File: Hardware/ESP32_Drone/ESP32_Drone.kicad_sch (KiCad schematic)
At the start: 71 parts, among them J1 USB_C_Receptacle_USB2.0_16P, J2 Conn_01x02_Socket, J3 Conn_01x02_Socket, J4 Conn_01x02_Socket, J5 Conn_01x02_Socket, J6 Conn_01x02_Socket, Q1 AO3401A, Q2 SS8050, Q3 SS8050, Q4 AO3400A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

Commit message: JCSC field added.
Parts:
- C1, C12: LCSC (none) -> C15850
- C10: LCSC (none) -> C45783
- C11, C13, C14, C15, C16, C4, C6, C8, C9: LCSC (none) -> C49678
- C2: LCSC (none) -> C1740
- C3: LCSC (none) -> C1806
- C5: LCSC (none) -> C1822
- C7: LCSC (none) -> C1653
- D1: LCSC (none) -> C8599
- D10, D11, D8, D9: LCSC (none) -> C8598
- D2: LCSC (none) -> C2286
- D3: LCSC (none) -> C2297
- J1: LCSC (none) -> C165948
- J2: LCSC (none) -> C166021
- Q1: LCSC (none) -> C15127
- Q2, Q3: LCSC (none) -> C181090
- Q4, Q5, Q6, Q7: LCSC (none) -> C20917
- R10, R11: LCSC (none) -> C21189
- R12, R13, R16, R21, R23, R25, R27, R28, R29: LCSC (none) -> C25804
- R14, R15: LCSC (none) -> C4184
- R17: LCSC (none) -> C22978
- R18, R19: LCSC (none) -> C4182
- R20, R22, R24, R26: LCSC (none) -> C21190
- R3, R4, R5, R6: LCSC (none) -> C25803
- R30, R31: LCSC (none) -> C23186
- R7: value 2k -> 1k; LCSC (none) -> C22706
- R8: value 22.1k -> 22k; LCSC (none) -> C25879
- R9: value 47.5k -> 47k; LCSC (none) -> C25819
- SW1: LCSC (none) -> JS102011SAQN
- U1: LCSC (none) -> C89366
- U2: LCSC (none) -> C2652470
- U3: LCSC (none) -> C24112
- U4: LCSC (none) -> C473012
- U5: LCSC (none) -> C16581

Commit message: PCB layout v1.0
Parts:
- C7: LCSC C1653 -> C107146
- D1: LCSC C8599 -> C8678
- D10, D11, D8, D9: LCSC C8598 -> C50645
- D3: LCSC C2297 -> C12624
- J2: LCSC C166021 -> C173752
- R18, R19: value 1.3k -> 1k; LCSC C4182 -> C21190
- R7: LCSC C22706 -> C21190
- R8: LCSC C25879 -> C23344
- SW1: LCSC JS102011SAQN -> C221660
- U1: LCSC C89366 -> C29613
- U2: LCSC C2652470 -> C964632
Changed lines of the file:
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@@
 			)
 		)
-		(property "LCSC" "C8598"
+		(property "LCSC" "C50645 "
 			(at 54.61 224.79 90)
 			(hide yes)
@@
 			)
 		)
-		(property "LCSC" "C2297"
+		(property "LCSC" "C12624"
 			(at 285.75 48.26 0)
 			(hide yes)
@@
 			)
 		)
-		(property "Value" "1.3k"
+		(property "Value" "1k"
 			(at 302.26 41.91 90)
 			(show_name no)
@@
 			)
 		)
-		(property "LCSC" "C4182"
+		(property "LCSC" "C21190"
 			(at 302.26 45.72 90)
 			(hide yes)
@@
 			)
 		)
-		(property "LCSC" "C8598"
+		(property "LCSC" "C50645 "
 			(at 250.19 224.79 90)
 			(hide yes)
@@
 			)
 		)
-		(property "LCSC" "C8598"
+		(property "LCSC" "C50645 "
 			(at 189.23 224.79 90)
 			(hide yes)
@@
 			)
 		)
-		(property "LCSC" "C1653"
+		(property "LCSC" "C107146 "
 			(at 224.79 127 0)
 			(hide yes)
@@
 			)
 		)
-		(property "LCSC" "C22706"
+		(property "LCSC" "C21190"
 			(at 46.99 114.3 90)
 			(hide yes)
@@
 			)
 		)
-		(property "LCSC" "C8598"
+		(property "LCSC" "C50645 "
 			(at 121.92 226.06 90)
 			(hide yes)
@@
 			)
 		)
-		(property "Value" "1.3k"
+		(property "Value" "1k"
 			(at 295.91 44.45 90)
 			(show_name no)
@@
 			)
 		)
-		(property "LCSC" "C4182"
+		(property "LCSC" "C21190"
 			(at 295.91 48.26 90)
 			(hide yes)
@@
 			)
 		)
-		(property "LCSC" "C25879"
+		(property "LCSC" "C23344"
 			(at 30.48 120.65 0)
 			(hide yes)
@@
 			)
 		)
-		(property "LCSC" "JS102011SAQN"
+		(property "LCSC" "C221660 "
 			(at 251.46 46.99 0)
 			(hide yes)
@@
 			)
 		)
-		(property "LCSC" "C8599"
+		(property "LCSC" "C8678"
 			(at 114.3 44.45 0)
 			(hide yes)
@@
 			)
 		)
-		(property "LCSC" "C2652470"
+		(property "LCSC" "C964632"
 			(at 66.04 142.24 0)
 			(hide yes)
@@
 			)
 		)
-		(property "LCSC" "C166021"
+		(property "LCSC" "C173752"
 			(at 369.57 40.64 0)
 			(hide yes)
@@
 			)
 		)
-		(property "LCSC" "C89366"
+		(property "LCSC" "C29613 "
 			(at 152.4 46.99 0)
 			(hide yes)

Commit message: JCSC numbers updated.
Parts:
- C2: LCSC C1740 -> C1743
- C3: LCSC C1806 -> C377773
- C5: LCSC C1822 -> C1779
- C7: LCSC C107146 -> C28260
- D3: LCSC C12624 -> C2290
- Q2, Q3: LCSC C181090 -> C2150
- R8: LCSC C23344 -> C31850
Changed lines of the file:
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@@
 			)
 		)
-		(property "LCSC" "C12624"
+		(property "LCSC" "C2290"
 			(at 285.75 48.26 0)
 			(hide yes)
@@
 			)
 		)
-		(property "LCSC" "C1740"
+		(property "LCSC" "C1743"
 			(at 163.83 53.34 0)
 			(hide yes)
@@
 			)
 		)
-		(property "LCSC" "C107146 "
+		(property "LCSC" "C28260"
 			(at 224.79 127 0)
 			(hide yes)
@@
 			)
 		)
-		(property "LCSC" "C181090"
+		(property "LCSC" "C2150"
 			(at 132.08 158.75 0)
 			(hide yes)
@@
 			)
 		)
-		(property "LCSC" "C181090"
+		(property "LCSC" "C2150"
 			(at 132.08 134.62 0)
 			(hide yes)
@@
 			)
 		)
-		(property "LCSC" "C1806"
+		(property "LCSC" "C377773"
 			(at 175.26 48.26 0)
 			(hide yes)
@@
 			)
 		)
-		(property "LCSC" "C23344"
+		(property "LCSC" "C31850"
 			(at 30.48 120.65 0)
 			(hide yes)
@@
 			)
 		)
-		(property "LCSC" "C1822"
+		(property "LCSC" "C1779"
 			(at 71.12 96.52 0)
 			(hide yes)

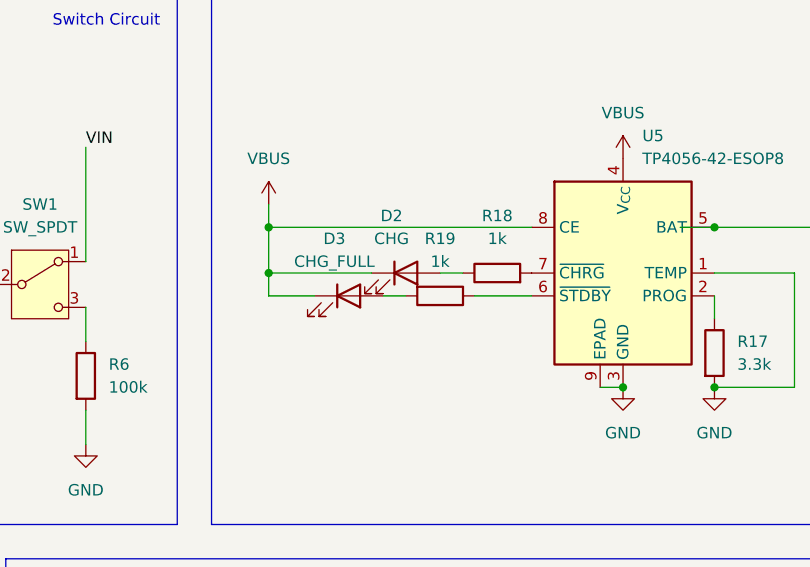
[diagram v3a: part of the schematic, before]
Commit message: Fixed charger LEDs.
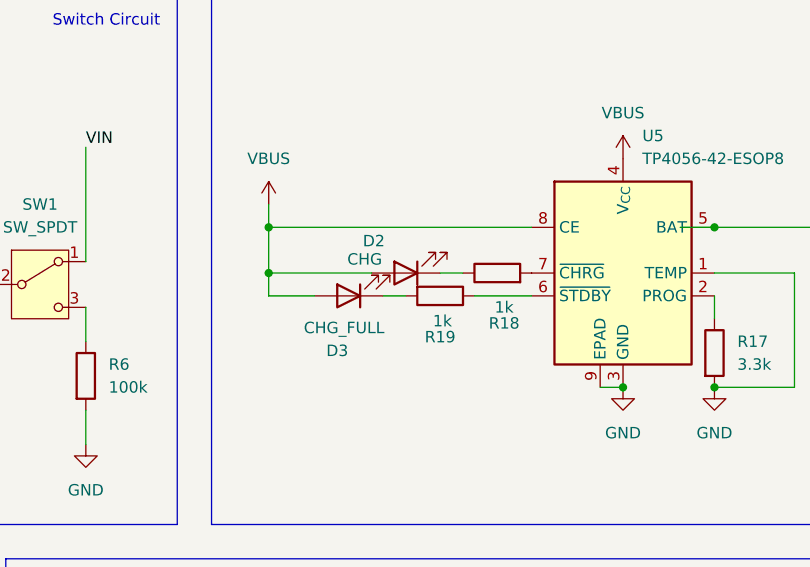
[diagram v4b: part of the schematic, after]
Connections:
- net VBUS: now also D2.2 (A), D3.2 (A); no longer D2.1 (K), D3.1 (K)
- net at R19.2: now also D3.1 (K); no longer D3.2 (A)
- net at R18.1: now also D2.1 (K); no longer D2.2 (A)
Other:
- moved on the sheet: D2, D3
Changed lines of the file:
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@@
 	(symbol
 		(lib_id "Device:LED")
-		(at 285.75 48.26 0)
+		(at 285.75 48.26 180)
 		(unit 1)
 		(body_style 1)
@@
 		(in_pos_files yes)
 		(dnp no)
-		(fields_autoplaced yes)
 		(property "Reference" "D3"
-			(at 284.1625 41.91 0)
+			(at 284.48 54.356 0)
 			(show_name no)
 			(do_not_autoplace no)
@@
 		)
 		(property "Value" "CHG_FULL"
-			(at 284.1625 44.45 0)
+			(at 285.242 51.816 0)
 			(show_name no)
 			(do_not_autoplace no)
@@
 		(in_pos_files yes)
 		(dnp no)
-		(fields_autoplaced yes)
 		(property "Reference" "R18"
-			(at 302.26 39.37 90)
+			(at 303.022 51.308 90)
 			(show_name no)
 			(do_not_autoplace no)
@@
 		)
 		(property "Value" "1k"
-			(at 302.26 41.91 90)
+			(at 303.022 49.53 90)
 			(show_name no)
 			(do_not_autoplace no)
@@
 	(symbol
 		(lib_id "Device:LED")
-		(at 292.1 45.72 0)
+		(at 292.1 45.72 180)
 		(unit 1)
 		(body_style 1)
@@
 		(in_pos_files yes)
 		(dnp no)
-		(fields_autoplaced yes)
 		(property "Reference" "D2"
-			(at 290.5125 39.37 0)
+			(at 288.544 42.164 0)
 			(show_name no)
 			(do_not_autoplace no)
@@
 		)
 		(property "Value" "CHG"
-			(at 290.5125 41.91 0)
+			(at 287.528 44.196 0)
 			(show_name no)
 			(do_not_autoplace no)
@@
 		(in_pos_files yes)
 		(dnp no)
-		(fields_autoplaced yes)
 		(property "Reference" "R19"
-			(at 295.91 41.91 90)
+			(at 295.91 52.832 90)
 			(show_name no)
 			(do_not_autoplace no)
@@
 		)
 		(property "Value" "1k"
-			(at 295.91 44.45 90)
+			(at 296.164 51.054 90)
 			(show_name no)
 			(do_not_autoplace no)
